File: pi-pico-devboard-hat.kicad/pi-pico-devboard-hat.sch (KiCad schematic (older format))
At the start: 14 parts, among them J1 Conn_01x24_Male, J2 I2C, J3 SDA_UP, J4 SCL_UP, P1 Conn_02x20_Odd_Even, SW1 SW_Reset, U1 Pico

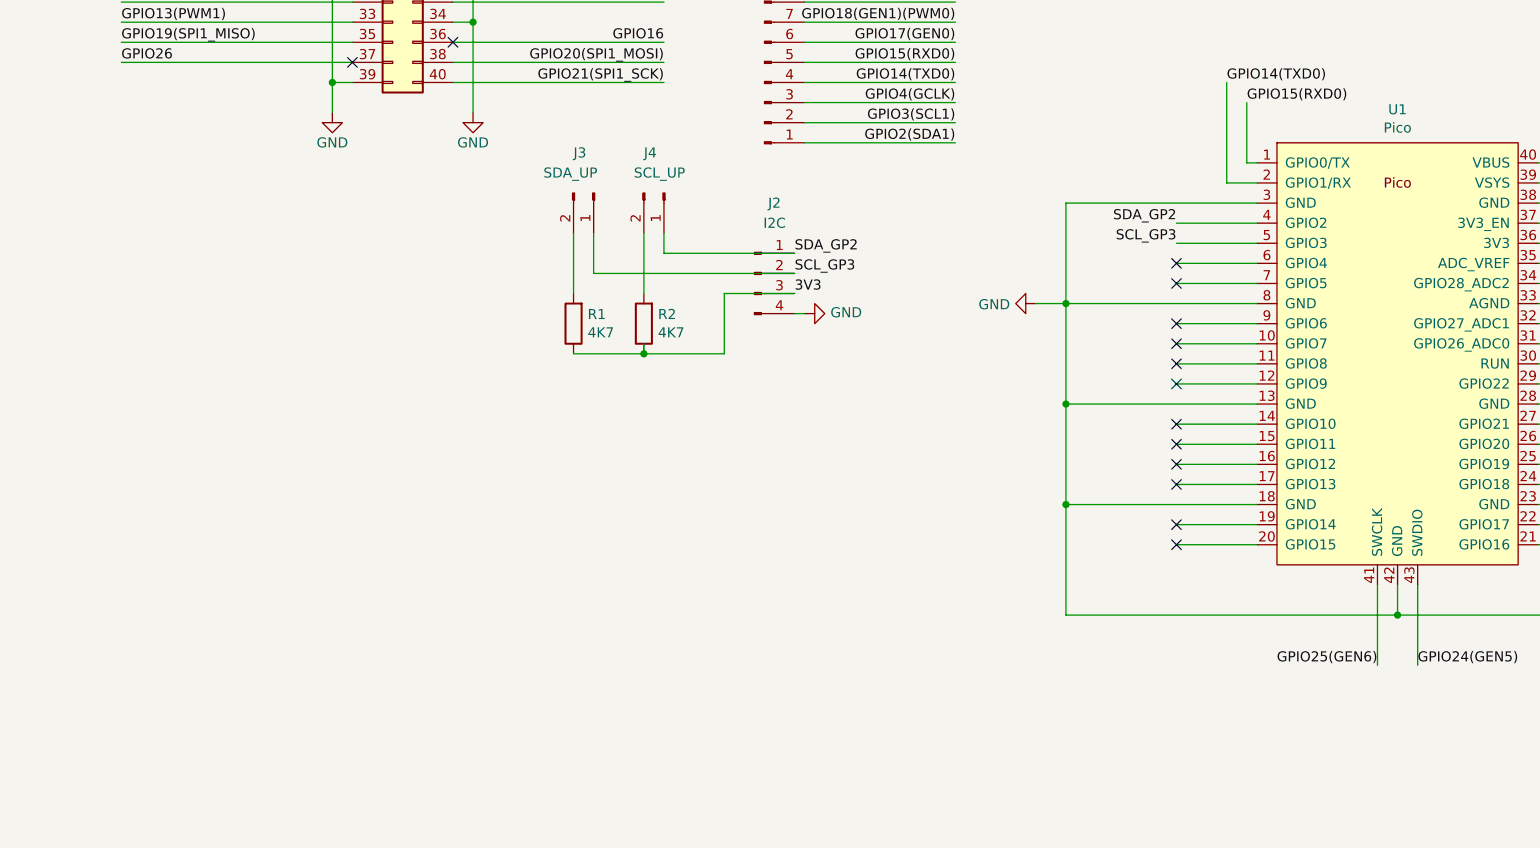
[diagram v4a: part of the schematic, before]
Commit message: Rev 4: added SPI1-connector
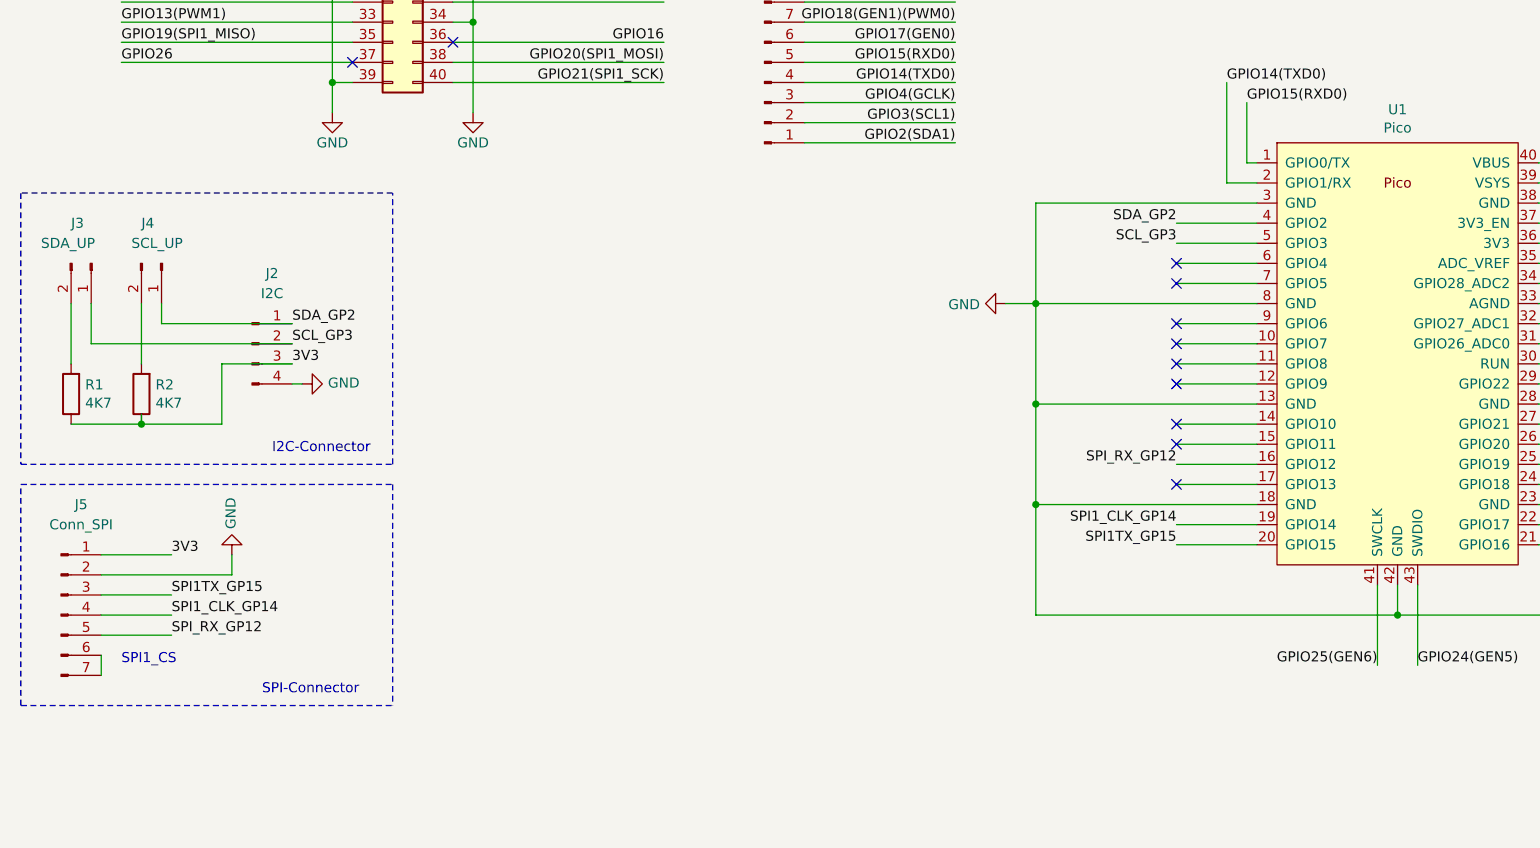
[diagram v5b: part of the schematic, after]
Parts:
- added J5: Conn_SPI, Connector_PinHeader_2.54mm:PinHeader_1x07_P2.54mm_Vertical, symbol Connector:Conn_01x07_Male
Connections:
- net 3V3: now also J5.1 (Pin_1)
- net GND: now also J5.2 (Pin_2)
- net SPI_RX_GP12: now reaches U1.16 (GPIO12)
- net SPI_RX_GP12: now also J5.5 (Pin_5)
- net SPI1_CLK_GP14: now reaches U1.19 (GPIO14)
- net SPI1_CLK_GP14: now also J5.4 (Pin_4)
- net SPI1TX_GP15: now reaches U1.20 (GPIO15)
- net SPI1TX_GP15: now also J5.3 (Pin_3)
- new net: J5.6 (Pin_6), J5.7 (Pin_7)
- no-connect marks 26 -> 23
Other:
- note added: "I2C-Connector"
- note added: "SPI-Connector"
- note added: "SPI1_CS"
- moved on the sheet: J2, J3, J4, R1, R2
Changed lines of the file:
@@
 Sheet 1 1
 Title "pi-pico-devboard-hat"
-Date "2021-03-18"
-Rev "3"
+Date "2021-03-22"
+Rev "4"
 Comp "Bernhard Bablok"
 Comment1 "https://github.com/bablokb/pi-pico-devboard-hat"
@@
 L power:GND #PWR05
 U 1 1 6050FECC
-P 5800 4100
-F 0 "#PWR05" H 5800 3850 50  0001 C CNN
-F 1 "GND" V 5805 3972 50  0000 R CNN
-F 2 "" H 5800 4100 50  0001 C CNN
-F 3 "" H 5800 4100 50  0001 C CNN
-	1    5800 4100
+P 5650 4100
+F 0 "#PWR05" H 5650 3850 50  0001 C CNN
+F 1 "GND" V 5655 3972 50  0000 R CNN
+F 2 "" H 5650 4100 50  0001 C CNN
+F 3 "" H 5650 4100 50  0001 C CNN
+	1    5650 4100
 	0    1    1    0
 $EndComp
 Wire Wire Line
-	5950 3600 5950 4100
-Connection ~ 5950 4100
-Wire Wire Line
-	5950 4100 5800 4100
-Wire Wire Line
-	5950 4100 5950 4600
-Connection ~ 5950 4600
+	5800 3600 5800 4100
+Connection ~ 5800 4100
+Wire Wire Line
+	5800 4100 5650 4100
+Wire Wire Line
+	5800 4100 5800 4600
+Connection ~ 5800 4600
 $Comp
 L power:+5V #PWR06
@@
 Wire Wire Line
 	9800 5650 9800 5100
-Connection ~ 7600 5650
 Wire Wire Line
 	7600 5650 7600 5500
@@
 	9800 4600 10050 4600
 Wire Wire Line
-	7600 5650 5950 5650
-Wire Wire Line
-	5950 4600 5950 5100
-Connection ~ 5950 5100
-Wire Wire Line
-	5950 5100 5950 5650
+	5800 4600 5800 5100
+Connection ~ 5800 5100
+Wire Wire Line
+	5800 5100 5800 5650
 $Comp
 L power:PWR_FLAG #FLG0102
@@
 	6750 3500 6900 3500
 Wire Wire Line
-	5950 4600 6900 4600
-Wire Wire Line
-	5950 5100 6900 5100
-Wire Wire Line
-	5950 3600 6900 3600
-Wire Wire Line
-	5950 4100 6900 4100
-Wire Wire Line
 	6500 4700 6900 4700
 Wire Wire Line
@@
 NoConn ~ 6500 4700
 NoConn ~ 6500 4800
-NoConn ~ 6500 4900
 NoConn ~ 6500 5000
-NoConn ~ 6500 5200
-NoConn ~ 6500 5300
 NoConn ~ 8700 4000
 NoConn ~ 8700 4200
@@
 L Connector:Conn_01x04_Male J2
 U 1 1 6061A256
-P 4400 3950
-F 0 "J2" H 4500 4300 50  0000 C CNN
-F 1 "I2C" H 4500 4200 50  0000 C CNN
-F 2 "Connector_PinHeader_2.54mm:PinHeader_1x04_P2.54mm_Vertical" H 4400 3950 50  0001 C CNN
-F 3 "~" H 4400 3950 50  0001 C CNN
-	1    4400 3950
-	1    0    0    -1
-$EndComp
-Text Label 4600 3850 0    50   ~ 0
+P 1900 4300
+F 0 "J2" H 2000 4650 50  0000 C CNN
+F 1 "I2C" H 2000 4550 50  0000 C CNN
+F 2 "Connector_PinHeader_2.54mm:PinHeader_1x04_P2.54mm_Vertical" H 1900 4300 50  0001 C CNN
+F 3 "~" H 1900 4300 50  0001 C CNN
+	1    1900 4300
+	1    0    0    -1
+$EndComp
+Text Label 2100 4200 0    50   ~ 0
 SDA_GP2
 Text Label 6500 3700 2    50   ~ 0
 SDA_GP2
-Text Label 4600 3950 0    50   ~ 0
+Text Label 2100 4300 0    50   ~ 0
 SCL_GP3
 Text Label 6500 3800 2    50   ~ 0
 SCL_GP3
-Text Label 4600 4050 0    50   ~ 0
+Text Label 2100 4400 0    50   ~ 0
 3V3
 $Comp
 L power:GND #PWR0101
 U 1 1 6061BF4A
-P 4650 4150
-F 0 "#PWR0101" H 4650 3900 50  0001 C CNN
-F 1 "GND" V 4655 4022 50  0000 R CNN
-F 2 "" H 4650 4150 50  0001 C CNN
-F 3 "" H 4650 4150 50  0001 C CNN
-	1    4650 4150
+P 2150 4500
+F 0 "#PWR0101" H 2150 4250 50  0001 C CNN
+F 1 "GND" V 2155 4372 50  0000 R CNN
+F 2 "" H 2150 4500 50  0001 C CNN
+F 3 "" H 2150 4500 50  0001 C CNN
+	1    2150 4500
 	0    -1   -1   0
 $EndComp
 Wire Wire Line
-	4600 4150 4650 4150
+	2100 4500 2150 4500
 $Comp
 L Device:R R2
 U 1 1 6062584D
-P 3850 4200
-F 0 "R2" H 3780 4154 50  0000 R CNN
-F 1 "4K7" H 3780 4245 50  0000 R CNN
-F 2 "Resistor_THT:R_Axial_DIN0207_L6.3mm_D2.5mm_P7.62mm_Horizontal" V 3780 4200 50  0001 C CNN
-F 3 "~" H 3850 4200 50  0001 C CNN
-	1    3850 4200
+P 1350 4550
+F 0 "R2" H 1280 4504 50  0000 R CNN
+F 1 "4K7" H 1280 4595 50  0000 R CNN
+F 2 "Resistor_THT:R_Axial_DIN0207_L6.3mm_D2.5mm_P7.62mm_Horizontal" V 1280 4550 50  0001 C CNN
+F 3 "~" H 1350 4550 50  0001 C CNN
+	1    1350 4550
 	-1   0    0    1
 $EndComp
@@
 L Device:R R1
 U 1 1 60626297
-P 3500 4200
-F 0 "R1" H 3430 4154 50  0000 R CNN
-F 1 "4K7" H 3430 4245 50  0000 R CNN
-F 2 "Resistor_THT:R_Axial_DIN0207_L6.3mm_D2.5mm_P7.62mm_Horizontal" V 3430 4200 50  0001 C CNN
-F 3 "~" H 3500 4200 50  0001 C CNN
-	1    3500 4200
+P 1000 4550
+F 0 "R1" H 930 4504 50  0000 R CNN
+F 1 "4K7" H 930 4595 50  0000 R CNN
+F 2 "Resistor_THT:R_Axial_DIN0207_L6.3mm_D2.5mm_P7.62mm_Horizontal" V 930 4550 50  0001 C CNN
+F 3 "~" H 1000 4550 50  0001 C CNN
+	1    1000 4550
 	-1   0    0    1
 $EndComp
@@
 L Connector:Conn_01x02_Male J3
 U 1 1 60626EA3
-P 3600 3550
-F 0 "J3" V 3400 3450 50  0000 L CNN
-F 1 "SDA_UP" V 3500 3300 50  0000 L CNN
-F 2 "Connector_PinHeader_2.54mm:PinHeader_1x02_P2.54mm_Vertical" H 3600 3550 50  0001 C CNN
-F 3 "~" H 3600 3550 50  0001 C CNN
-	1    3600 3550
+P 1100 3900
+F 0 "J3" V 900 3800 50  0000 L CNN
+F 1 "SDA_UP" V 1000 3650 50  0000 L CNN
+F 2 "Connector_PinHeader_2.54mm:PinHeader_1x02_P2.54mm_Vertical" H 1100 3900 50  0001 C CNN
+F 3 "~" H 1100 3900 50  0001 C CNN
+	1    1100 3900
 	0    1    1    0
 $EndComp
@@
 L Connector:Conn_01x02_Male J4
 U 1 1 606291D7
-P 3950 3550
-F 0 "J4" V 3750 3450 50  0000 L CNN
-F 1 "SCL_UP" V 3850 3400 50  0000 L CNN
-F 2 "Connector_PinHeader_2.54mm:PinHeader_1x02_P2.54mm_Vertical" H 3950 3550 50  0001 C CNN
-F 3 "~" H 3950 3550 50  0001 C CNN
-	1    3950 3550
+P 1450 3900
+F 0 "J4" V 1250 3800 50  0000 L CNN
+F 1 "SCL_UP" V 1350 3750 50  0000 L CNN
+F 2 "Connector_PinHeader_2.54mm:PinHeader_1x02_P2.54mm_Vertical" H 1450 3900 50  0001 C CNN
+F 3 "~" H 1450 3900 50  0001 C CNN
+	1    1450 3900
 	0    1    1    0
 $EndComp
 Wire Wire Line
-	4600 3850 3950 3850
-Wire Wire Line
-	3950 3850 3950 3750
-Wire Wire Line
-	4600 3950 3600 3950
-Wire Wire Line
-	3600 3950 3600 3750
-Wire Wire Line
-	3500 3750 3500 4050
-Wire Wire Line
-	3850 3750 3850 4050
-Wire Wire Line
-	4600 4050 4250 4050
-Wire Wire Line
-	4250 4050 4250 4350
-Wire Wire Line
-	4250 4350 3850 4350
-Wire Wire Line
-	3850 4300 3850 4350
-Wire Wire Line
-	3850 4350 3500 4350
-Connection ~ 3850 4350
+	2100 4200 1450 4200
+Wire Wire Line
+	1450 4200 1450 4100
+Wire Wire Line
+	2100 4300 1100 4300
+Wire Wire Line
+	1100 4300 1100 4100
+Wire Wire Line
+	1000 4100 1000 4400
+Wire Wire Line
+	1350 4100 1350 4400
+Wire Wire Line
+	2100 4400 1750 4400
+Wire Wire Line
+	1750 4400 1750 4700
+Wire Wire Line
+	1750 4700 1350 4700
+Wire Wire Line
+	1350 4650 1350 4700
+Wire Wire Line
+	1350 4700 1000 4700
+Connection ~ 1350 4700
+$Comp
+L Connector:Conn_01x07_Male J5
+U 1 1 605903A9
+P 950 5650
+F 0 "J5" H 1050 6200 50  0000 C CNN
+F 1 "Conn_SPI" H 1050 6100 50  0000 C CNN
+F 2 "Connector_PinHeader_2.54mm:PinHeader_1x07_P2.54mm_Vertical" H 950 5650 50  0001 C CNN
+F 3 "~" H 950 5650 50  0001 C CNN
+	1    950  5650
+	1    0    0    -1
+$EndComp
+Text Label 1500 5350 0    50   ~ 0
+3V3
+$Comp
+L power:GND #PWR08
+U 1 1 60592C62
+P 1800 5350
+F 0 "#PWR08" H 1800 5100 50  0001 C CNN
+F 1 "GND" V 1805 5222 50  0000 R CNN
+F 2 "" H 1800 5350 50  0001 C CNN
+F 3 "" H 1800 5350 50  0001 C CNN
+	1    1800 5350
+	-1   0    0    1
+$EndComp
+Text Label 1500 5550 0    50   ~ 0
+SPI1TX_GP15
+Text Label 1500 5650 0    50   ~ 0
+SPI1_CLK_GP14
+Text Label 1500 5750 0    50   ~ 0
+SPI_RX_GP12
+Wire Wire Line
+	1150 5350 1500 5350
+Wire Wire Line
+	1800 5450 1800 5350
+Wire Wire Line
+	1150 5450 1800 5450
+Wire Wire Line
+	1150 5550 1500 5550
+Wire Wire Line
+	1150 5650 1500 5650
+Wire Wire Line
+	1150 5750 1500 5750
+Wire Wire Line
+	1150 5950 1150 5850
+Text Notes 1250 5900 0    50   ~ 0
+SPI1_CS
+Text Label 6500 5300 2    50   ~ 0
+SPI1TX_GP15
+Text Label 6500 5200 2    50   ~ 0
+SPI1_CLK_GP14
+Text Label 6500 4900 2    50   ~ 0
+SPI_RX_GP12
+Wire Wire Line
+	5800 5100 6900 5100
+Wire Wire Line
+	5800 4600 6900 4600
+Wire Wire Line
+	5800 4100 6900 4100
+Wire Wire Line
+	5800 3600 6900 3600
+Wire Wire Line
+	5800 5650 7600 5650
+Connection ~ 7600 5650
+Wire Notes Line
+	750  3550 750  4900
+Wire Notes Line
+	750  4900 2600 4900
+Wire Notes Line
+	2600 4900 2600 3550
+Wire Notes Line
+	2600 3550 750  3550
+Wire Notes Line
+	750  6100 750  5000
+Text Notes 2000 4850 0    50   ~ 0
+I2C-Connector
+Text Notes 1950 6050 0    50   ~ 0
+SPI-Connector
+Wire Notes Line
+	2600 5000 2600 6100
+Wire Notes Line
+	750  5000 2600 5000
+Wire Notes Line
+	750  6100 2600 6100
 $EndSCHEMATC

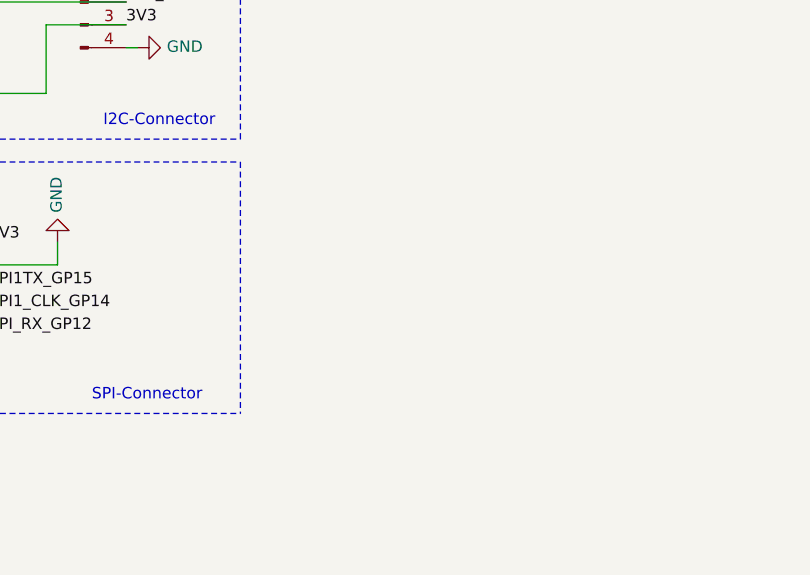
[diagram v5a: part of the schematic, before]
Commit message: Rev 5: added external connector
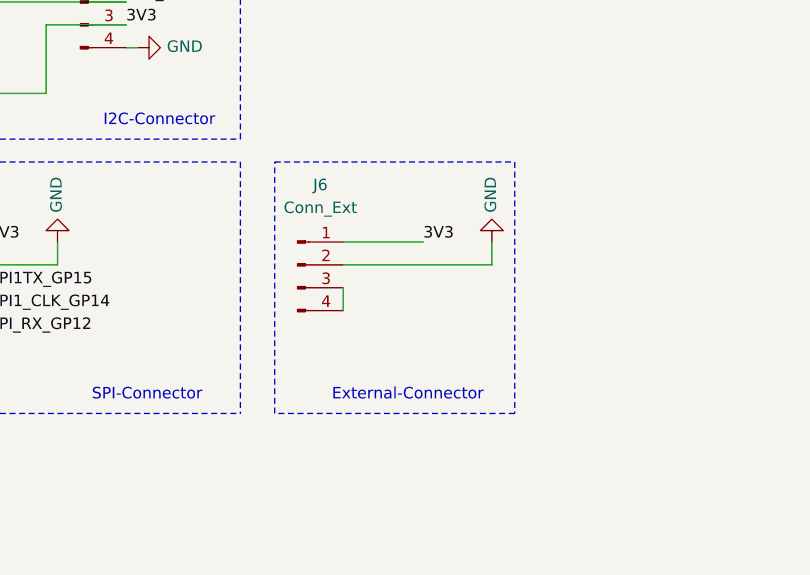
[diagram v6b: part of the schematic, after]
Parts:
- added J6: Conn_Ext, Connector_PinHeader_2.54mm:PinHeader_1x04_P2.54mm_Vertical, symbol Connector:Conn_01x04_Male
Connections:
- net 3V3: now also J6.1 (Pin_1)
- net GND: now also J6.2 (Pin_2)
- new net: J6.3 (Pin_3), J6.4 (Pin_4)
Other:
- note added: "External-Connector"
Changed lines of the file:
@@
 Sheet 1 1
 Title "pi-pico-devboard-hat"
-Date "2021-03-22"
-Rev "4"
+Date "2021-03-23"
+Rev "5"
 Comp "Bernhard Bablok"
 Comment1 "https://github.com/bablokb/pi-pico-devboard-hat"
@@
 Wire Notes Line
 	750  6100 2600 6100
+$Comp
+L Connector:Conn_01x04_Male J6
+U 1 1 605A6142
+P 2850 5450
+F 0 "J6" H 2950 5800 50  0000 C CNN
+F 1 "Conn_Ext" H 2950 5700 50  0000 C CNN
+F 2 "Connector_PinHeader_2.54mm:PinHeader_1x04_P2.54mm_Vertical" H 2850 5450 50  0001 C CNN
+F 3 "~" H 2850 5450 50  0001 C CNN
+	1    2850 5450
+	1    0    0    -1
+$EndComp
+Text Label 3400 5350 0    50   ~ 0
+3V3
+$Comp
+L power:GND #PWR0102
+U 1 1 605AA8EF
+P 3700 5350
+F 0 "#PWR0102" H 3700 5100 50  0001 C CNN
+F 1 "GND" V 3705 5222 50  0000 R CNN
+F 2 "" H 3700 5350 50  0001 C CNN
+F 3 "" H 3700 5350 50  0001 C CNN
+	1    3700 5350
+	-1   0    0    1
+$EndComp
+Wire Wire Line
+	3050 5350 3400 5350
+Wire Wire Line
+	3700 5450 3700 5350
+Wire Wire Line
+	3050 5450 3700 5450
+Wire Wire Line
+	3050 5650 3050 5550
+Wire Notes Line
+	2750 5000 3800 5000
+Wire Notes Line
+	3800 5000 3800 6100
+Wire Notes Line
+	3800 6100 2750 6100
+Wire Notes Line
+	2750 6100 2750 5000
+Text Notes 3000 6050 0    50   ~ 0
+External-Connector
 $EndSCHEMATC

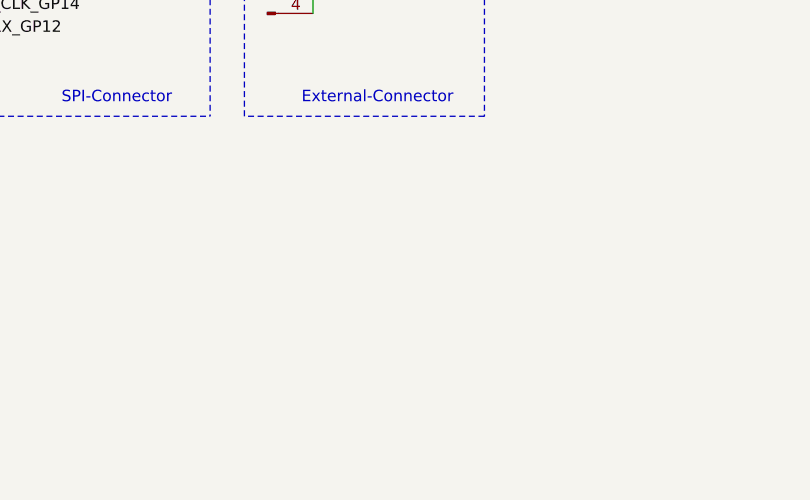
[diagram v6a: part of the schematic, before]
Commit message: Rev 6: added buttons
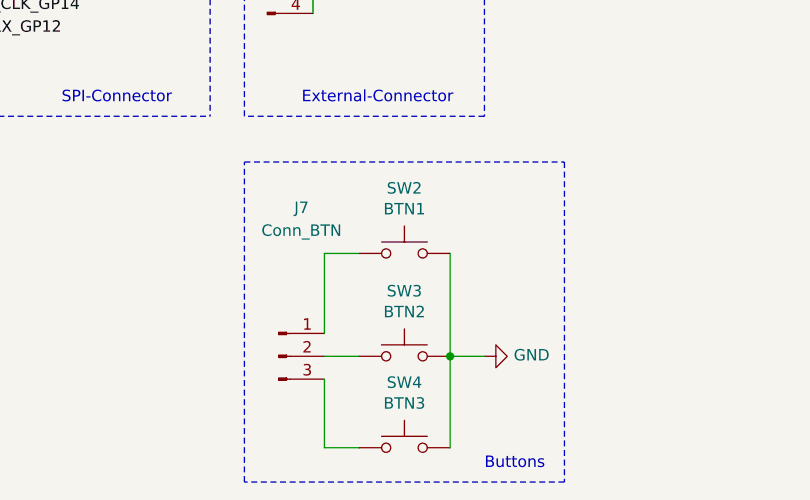
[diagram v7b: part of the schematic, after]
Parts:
- added J7: Conn_BTN, Connector_PinHeader_2.54mm:PinHeader_1x03_P2.54mm_Vertical, symbol Connector:Conn_01x03_Male
- added SW2: BTN1, user:SW_PUSH_SLIM_1x4, symbol Switch:SW_Push
- added SW3: BTN2, user:SW_PUSH_SLIM_1x4, symbol Switch:SW_Push
- added SW4: BTN3, user:SW_PUSH_SLIM_1x4, symbol Switch:SW_Push
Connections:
- net GND: now also SW2.2, SW3.2, SW4.2
- new net: J7.1 (Pin_1), SW2.1
- new net: J7.2 (Pin_2), SW3.1
- new net: J7.3 (Pin_3), SW4.1
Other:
- note added: "Buttons"
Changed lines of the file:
@@
 Title "pi-pico-devboard-hat"
 Date "2021-03-23"
-Rev "5"
+Rev "6"
 Comp "Bernhard Bablok"
 Comment1 "https://github.com/bablokb/pi-pico-devboard-hat"
@@
 Text Notes 3000 6050 0    50   ~ 0
 External-Connector
+$Comp
+L Switch:SW_Push SW2
+U 1 1 605E1ED2
+P 3450 6700
+F 0 "SW2" H 3450 6985 50  0000 C CNN
+F 1 "BTN1" H 3450 6894 50  0000 C CNN
+F 2 "user:SW_PUSH_SLIM_1x4" H 3450 6900 50  0001 C CNN
+F 3 "~" H 3450 6900 50  0001 C CNN
+	1    3450 6700
+	1    0    0    -1
+$EndComp
+$Comp
+L Switch:SW_Push SW3
+U 1 1 605EB865
+P 3450 7150
+F 0 "SW3" H 3450 7435 50  0000 C CNN
+F 1 "BTN2" H 3450 7344 50  0000 C CNN
+F 2 "user:SW_PUSH_SLIM_1x4" H 3450 7350 50  0001 C CNN
+F 3 "~" H 3450 7350 50  0001 C CNN
+	1    3450 7150
+	1    0    0    -1
+$EndComp
+$Comp
+L Switch:SW_Push SW4
+U 1 1 605EBC25
+P 3450 7550
+F 0 "SW4" H 3450 7835 50  0000 C CNN
+F 1 "BTN3" H 3450 7744 50  0000 C CNN
+F 2 "user:SW_PUSH_SLIM_1x4" H 3450 7750 50  0001 C CNN
+F 3 "~" H 3450 7750 50  0001 C CNN
+	1    3450 7550
+	1    0    0    -1
+$EndComp
+$Comp
+L Connector:Conn_01x03_Male J7
+U 1 1 605EC64E
+P 2900 7150
+F 0 "J7" H 3000 7800 50  0000 C CNN
+F 1 "Conn_BTN" H 3000 7700 50  0000 C CNN
+F 2 "Connector_PinHeader_2.54mm:PinHeader_1x03_P2.54mm_Vertical" H 2900 7150 50  0001 C CNN
+F 3 "~" H 2900 7150 50  0001 C CNN
+	1    2900 7150
+	1    0    0    -1
+$EndComp
+$Comp
+L power:GND #PWR09
+U 1 1 605ED18C
+P 3800 7150
+F 0 "#PWR09" H 3800 6900 50  0001 C CNN
+F 1 "GND" V 3805 7022 50  0000 R CNN
+F 2 "" H 3800 7150 50  0001 C CNN
+F 3 "" H 3800 7150 50  0001 C CNN
+	1    3800 7150
+	0    -1   -1   0
+$EndComp
+Wire Wire Line
+	3650 6700 3650 7150
+Connection ~ 3650 7150
+Wire Wire Line
+	3650 7150 3650 7550
+Wire Wire Line
+	3100 7050 3100 6700
+Wire Wire Line
+	3100 7250 3100 7550
+Wire Wire Line
+	3100 6700 3250 6700
+Wire Wire Line
+	3100 7150 3250 7150
+Wire Wire Line
+	3100 7550 3250 7550
+Wire Wire Line
+	3650 7150 3800 7150
+Wire Notes Line
+	2750 6300 4150 6300
+Wire Notes Line
+	4150 6300 4150 7700
+Wire Notes Line
+	4150 7700 2750 7700
+Wire Notes Line
+	2750 7700 2750 6300
+Text Notes 3800 7650 0    50   ~ 0
+Buttons
 $EndSCHEMATC
